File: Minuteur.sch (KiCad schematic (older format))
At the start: 40 parts, among them J1 ICSP, J2 Screw_Terminal_1x02, J3 Piezo, J4 Inputs, J5 Data, J6 USB_OTG, J7 Screw_Terminal_1x03, J8 Outputs, Q1 BC818-40, SW1 Rotary_Encoder_Switch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

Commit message: Commit last changes (probably Kicad wanting me to update footprints library) before switching to V2, with a new shaape for the board.
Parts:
- removed AFF1: CC56-12, Displays_7-Segment:Cx56-12, symbol CC56-12
- removed C1, C4, C5: 100n, Capacitors_SMD:C_0805, symbol C
- removed C2, C3: 47u, Capacitors_SMD:CP_Elec_6.3x5.3, symbol CP
- removed D1, D4: D, Diodes_SMD:D_SOD-123, symbol D
- removed D2, D3: LED, LEDs:LED_0805, symbol LED
- removed J1: ICSP, Connectors:IDC_Header_Straight_6pins, symbol CONN_02X03
- removed J2: Screw_Terminal_1x02, Connectors:bornier2, symbol Screw_Terminal_1x02
- removed J3: Piezo, Pin_Headers:Pin_Header_Straight_1x02_Pitch2.54mm, symbol CONN_01X02
- removed J4: Inputs, Pin_Headers:Pin_Header_Straight_1x07_Pitch2.54mm, symbol CONN_01X07
- removed J5: Data, Pin_Headers:Pin_Header_Straight_1x06_Pitch2.54mm, symbol CONN_01X06
- removed J6: USB_OTG, Connectors:USB_Micro-B, symbol USB_OTG
- removed J7: Screw_Terminal_1x03, Connectors:bornier3, symbol Screw_Terminal_1x03
- removed J8: Outputs, Pin_Headers:Pin_Header_Straight_1x04_Pitch2.54mm, symbol Conn_01x04
- removed Q1: BC818-40, TO_SOT_Packages_SMD:SOT-23, symbol BC818-40
- removed R1, R11, R12, R4, R5, R7: 470, Resistors_SMD:R_0805, symbol R
- removed R10: 510, Resistors_SMD:R_0805, symbol R
- removed R2: 10K, Resistors_SMD:R_0805, symbol R
- removed R3, R8, R9: 1K, Resistors_SMD:R_0805, symbol R
- removed R6: 30K, Resistors_SMD:R_0805, symbol R
- removed RL1: RelaySongle240VAC10A, Relays_THT:Relay_SPDT_SANYOU_SRD_Series_Form_C, symbol RelaySongle240VAC10A
- removed SW1: Rotary_Encoder_Switch, Switches_perso:EC12_switch-RotaryEncoder, symbol Rotary_Encoder_Switch
- removed SW2, SW3: SW_Push_SPDT_2Leds, Switches_perso:SP86-THT-PushButton, symbol SW_Push_SPDT_2Leds
- removed U1: ATMEGA328P-AU, Housings_QFP:TQFP-32_7x7mm_Pitch0.8mm, symbol ATMEGA328P-AU
- removed U2: LD1117S50TR, TO_SOT_Packages_SMD:SOT-223-3Lead_TabPin2, symbol LD1117S50TR
- removed U3: MAX7219, Housings_SOIC:SOIC-24W_7.5x15.4mm_Pitch1.27mm, symbol MAX7219
- removed U4: PC817, Housings_DIP:DIP-4_W7.62mm_SMD, symbol PC817
- removed Y1: 16MHz, SMD_perso:Resonator_SMD-3pin_3213, symbol Crystal_GND2
- added C1, C4, C5: 100n, Capacitor_SMD:C_0805_2012Metric, symbol Device:C
- added C2, C3: 47u, symbol Device:CP
- added D1, D4: D, Diode_SMD:D_SOD-123, symbol Device:D
- added D2, D3: LED, LED_SMD:LED_0805_2012Metric, symbol Device:LED
- added J1: Screw_Terminal_01x02, symbol Connector:Screw_Terminal_01x02
- added J2: ICSP, symbol Connector_Generic:Conn_02x03_Odd_Even
- added J3: piezo, symbol Connector_Generic:Conn_01x02
- added J4: input, symbol Connector_Generic:Conn_01x07
- added J5: USB_OTG, symbol Connector:USB_OTG
- added J6: data, symbol Connector_Generic:Conn_01x06
- added J7: output, symbol Connector_Generic:Conn_01x04
- added J8: Screw_Terminal_01x03, symbol Connector:Screw_Terminal_01x03
- added Q1: BC818, Package_TO_SOT_SMD:SOT-23, symbol Transistor_BJT:BC818
- added R1, R11, R4, R5, R7: 470, symbol Device:R
- added R10: 510, symbol Device:R
- added R2: 10k, symbol Device:R
- added R3, R8, R9: 1k, symbol Device:R
- added R6: 30k, symbol Device:R
- added RL1: RelaySongle240VAC10A, symbol Switch_Perso:RelaySongle240VAC10A
- added SW1: Rotary_Encoder_Switch, symbol Device:Rotary_Encoder_Switch
- added SW2: SW_Push_SPDT_2Leds, symbol Switch_Perso:SW_Push_SPDT_2Leds
- added U1: ATmega328P-AU, Package_QFP:TQFP-32_7x7mm_P0.8mm, symbol MCU_Microchip_ATmega:ATmega328P-AU
- added U2: LD1117S50TR_SOT223, Package_TO_SOT_SMD:SOT-223-3_TabPin2, symbol Regulator_Linear:LD1117S50TR_SOT223
- added U3: MAX7219, symbol Driver_LED:MAX7219
- added U4: PC817, Package_DIP:DIP-4_W7.62mm, symbol Isolator:PC817
- added U5: CC56-12EWA, Display_7Segment:CA56-12EWA, symbol Display_Character:CC56-12EWA
- added Y1: 16MHz, symbol Device:Crystal_GND2
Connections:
- wire segments 126 -> 118
- no-connect marks 21 -> 16

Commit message: General layout done.
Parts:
- removed D2, D3: LED, LED_SMD:LED_0805_2012Metric, symbol Device:LED
- removed J4: input, symbol Connector_Generic:Conn_01x07
- removed J5: USB_OTG, symbol Connector:USB_OTG
- removed J6: data, symbol Connector_Generic:Conn_01x06
- removed R3: 1k, symbol Device:R
- added C1: 100n, Capacitor_SMD:C_0805_2012Metric, symbol Device:C
- added FID1, FID2, FID3, FID4, FID5, FID6: Fiducial, Fiducial:Fiducial_0.75mm_Mask1.5mm, symbol Mechanical:Fiducial
- added H1, H2, H3, H4: MountingHole, MountingHole:MountingHole_3.2mm_M3, symbol Mechanical:MountingHole
- added J4: Conn_01x10, Connector_PinHeader_2.54mm:PinHeader_1x10_P2.54mm_Vertical, symbol Connector_Generic:Conn_01x10
- C3: renamed from C2; footprint (none) -> Capacitor_SMD:CP_Elec_6.3x5.3
- C4: renamed from C3; footprint (none) -> Capacitor_SMD:CP_Elec_6.3x5.3
- J1: footprint (none) -> Connector_Phoenix_MSTB:PhoenixContact_MSTBVA_2,5_2-G-5,08_1x02_P5.08mm_Vertical
- J2: footprint (none) -> Connector_PinHeader_2.54mm:PinHeader_2x03_P2.54mm_Vertical
- J3: footprint (none) -> Connector_PinHeader_2.54mm:PinHeader_1x02_P2.54mm_Vertical
- J5: renamed from J7; footprint (none) -> Connector_PinHeader_2.54mm:PinHeader_1x04_P2.54mm_Vertical
- J6: renamed from J8; footprint (none) -> Connector_Phoenix_MSTB:PhoenixContact_MSTBVA_2,5_3-G-5,08_1x03_P5.08mm_Vertical
- R1, R2: footprint (none) -> Resistor_SMD:R_0805_2012Metric
- R10: renamed from R11; footprint (none) -> Resistor_SMD:R_0805_2012Metric
- R3: renamed from R4; footprint (none) -> Resistor_SMD:R_0805_2012Metric
- R4: renamed from R5; footprint (none) -> Resistor_SMD:R_0805_2012Metric
- R5: renamed from R6; footprint (none) -> Resistor_SMD:R_0805_2012Metric
- R6: renamed from R7; footprint (none) -> Resistor_SMD:R_0805_2012Metric
- R7: renamed from R8; footprint (none) -> Resistor_SMD:R_0805_2012Metric
- R8: renamed from R9; footprint (none) -> Resistor_SMD:R_0805_2012Metric
- R9: renamed from R10; footprint (none) -> Resistor_SMD:R_0805_2012Metric
- RL1: footprint (none) -> Relay_THT:Relay_SPDT_SANYOU_SRD_Series_Form_C
- SW1: footprint (none) -> Rotary_Encoder:RotaryEncoder_Alps_EC12E-Switch_Vertical_H20mm_CircularMountingHoles
- SW2: footprint (none) -> Switch_Perso:SP86-THT-PushButton
- U3: footprint (none) -> Package_SO:SOIC-24W_7.5x15.4mm_P1.27mm
- Y1: footprint (none) -> Crystal:Resonator_SMD_muRata_CSTxExxV-3Pin_3.0x1.1mm
- renumbered C1 to C2, C4 to C5, C5 to C6, D4 to D2
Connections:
- net labels added: +12V, A3, A4, A5, A6, A7, D0, D1, D6
- net labels removed: BTN_3, RXD, SCL, SDA, TXD, VCC
- wire segments 118 -> 96
- no-connect marks 16 -> 10
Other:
- moved on the sheet: D1, J6, R2

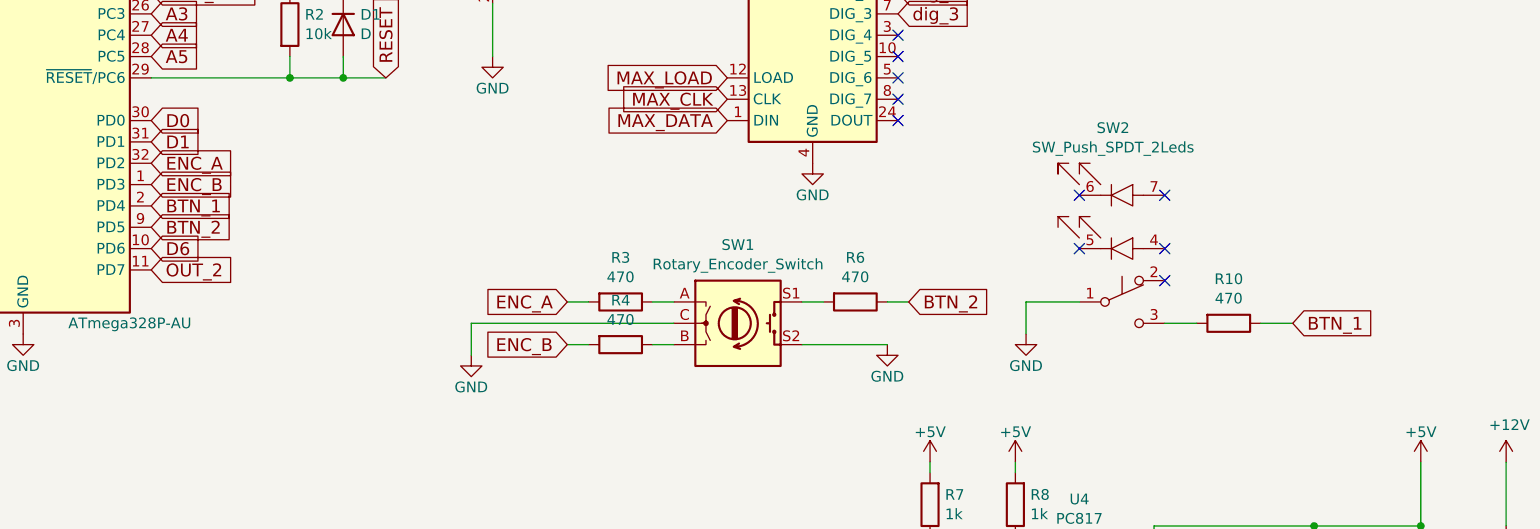
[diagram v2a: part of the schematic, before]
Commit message: Routing done. Maybe need to move down extension connectors a little. Also need to replace the piezo connector by a SMD one.
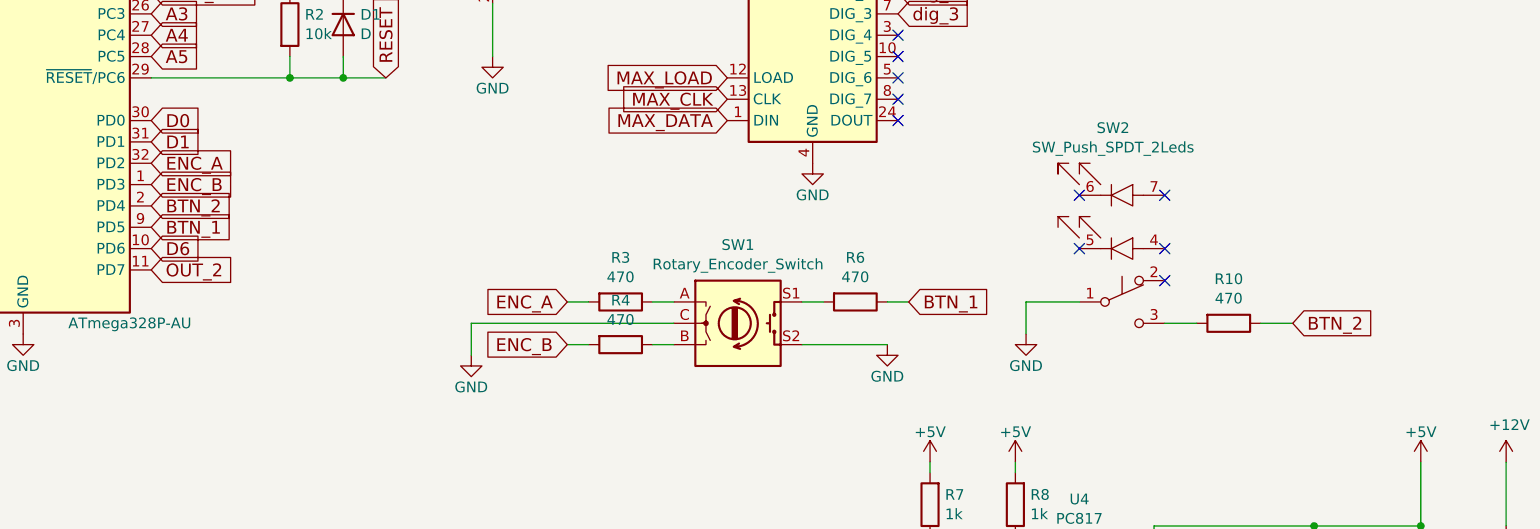
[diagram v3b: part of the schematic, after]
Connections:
- net BTN_1: now also R6.1, U1.9 (PD5); no longer R10.1, U1.2 (PD4)
- net BTN_2: now also R10.1, U1.2 (PD4); no longer R6.1, U1.9 (PD5)
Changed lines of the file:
@@
 ENC_A
 Text GLabel 3150 3800 2    60   Input ~ 0
-BTN_2
+BTN_1
 Text GLabel 3150 2500 2    60   Input ~ 0
 MAX_DATA
@@
 $EndComp
 Text GLabel 8500 4250 2    60   Input ~ 0
-BTN_1
+BTN_2
 $Comp
 L power:GND #PWR02
@@
 PIEZO_1
 Text GLabel 3150 3700 2    60   Input ~ 0
-BTN_1
+BTN_2
 $Comp
 L power:GND #PWR021
@@
 $EndComp
 $Comp
-L Connector_Generic:Conn_01x02 J3
-U 1 1 5EFB8BD6
-P 2050 5500
-F 0 "J3" H 2130 5492 50  0000 L CNN
-F 1 "piezo" H 2130 5401 50  0000 L CNN
-F 2 "Connector_PinHeader_2.54mm:PinHeader_1x02_P2.54mm_Vertical" H 2050 5500 50  0001 C CNN
-F 3 "~" H 2050 5500 50  0001 C CNN
-	1    2050 5500
-	1    0    0    -1
-$EndComp
-$Comp
 L Regulator_Linear:LD1117S50TR_SOT223 U2
 U 1 1 5EFBB817
@@
 Connection ~ 3350 6350
 Text GLabel 6700 4150 2    60   Input ~ 0
-BTN_2
+BTN_1
 Connection ~ 3800 2650
 $Comp
@@
 Wire Wire Line
 	1050 1600 1350 1600
+$Comp
+L Connector_Generic:Conn_01x02 J3
+U 1 1 5EFB8BD6
+P 2050 5500
+F 0 "J3" H 2130 5492 50  0000 L CNN
+F 1 "piezo" H 2130 5401 50  0000 L CNN
+F 2 "Connector_PinHeader_2.54mm:PinHeader_1x02_P2.54mm_Vertical" H 2050 5500 50  0001 C CNN
+F 3 "~" H 2050 5500 50  0001 C CNN
+	1    2050 5500
+	1    0    0    -1
+$EndComp
 $EndSCHEMATC

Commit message: All routing done, DRC ok.
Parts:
- removed J3: piezo, Connector_PinHeader_2.54mm:PinHeader_1x02_P2.54mm_Vertical, symbol Connector_Generic:Conn_01x02
- added U6: Piezo_sounder, IC_Perso:Murata_PKMCS0909_xxxxx, symbol Chip_Perso:Piezo_sounder
- R1: value 470 -> 1k
- R8: value 1k -> 470
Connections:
- net PIEZO_2: now also U6.2
- net at R1.1: now also U6.1
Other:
- moved on the sheet: R1
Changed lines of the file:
@@
 Text GLabel 3150 1700 2    60   Input ~ 0
 PIEZO_2
-Text GLabel 1350 5450 0    60   Input ~ 0
+Text GLabel 1950 5400 0    60   Input ~ 0
 PIEZO_1
 Text GLabel 3150 3700 2    60   Input ~ 0
@@
 	1    0    0    -1
 $EndComp
-Text GLabel 1350 5650 0    60   Input ~ 0
+Text GLabel 1950 5700 0    60   Input ~ 0
 PIEZO_2
 Wire Wire Line
@@
 Wire Wire Line
 	4950 2200 4950 2550
-Wire Wire Line
-	1350 5650 1800 5650
-Wire Wire Line
-	1800 5650 1800 5600
-Wire Wire Line
-	1800 5600 1850 5600
-Wire Wire Line
-	1350 5450 1450 5450
-Wire Wire Line
-	1750 5450 1800 5450
-Wire Wire Line
-	1800 5450 1800 5500
-Wire Wire Line
-	1800 5500 1850 5500
 Text GLabel 3150 1800 2    60   Input ~ 0
 PIEZO_1
@@
 P 7200 5100
 F 0 "R8" H 7130 5054 50  0000 R CNN
-F 1 "1k" H 7130 5145 50  0000 R CNN
+F 1 "470" H 7130 5145 50  0000 R CNN
 F 2 "Resistor_SMD:R_0805_2012Metric" V 7130 5100 50  0001 C CNN
 F 3 "~" H 7200 5100 50  0001 C CNN
@@
 Connection ~ 9100 5200
 $Comp
-L Device:R R1
-U 1 1 5EF81C42
-P 1600 5450
-F 0 "R1" V 1393 5450 50  0000 C CNN
-F 1 "470" V 1484 5450 50  0000 C CNN
-F 2 "Resistor_SMD:R_0805_2012Metric" V 1530 5450 50  0001 C CNN
-F 3 "~" H 1600 5450 50  0001 C CNN
-	1    1600 5450
-	0    1    1    0
-$EndComp
-$Comp
 L Device:C C5
 U 1 1 5EF86361
@@
 U 1 1 5EFADC83
 P 7500 5400
-F 0 "U4" H 7500 5725 50  0000 C CNN
-F 1 "PC817" H 7500 5634 50  0000 C CNN
+F 0 "U4" H 7300 5200 50  0000 C CNN
+F 1 "PC817" H 7600 5200 50  0000 C CNN
 F 2 "Package_DIP:DIP-4_W7.62mm" H 7300 5200 50  0001 L CIN
 F 3 "http://www.soselectronic.cz/a_info/resource/d/pc817.pdf" H 7500 5400 50  0001 L CNN
@@
 	1050 1600 1350 1600
 $Comp
-L Connector_Generic:Conn_01x02 J3
-U 1 1 5EFB8BD6
-P 2050 5500
-F 0 "J3" H 2130 5492 50  0000 L CNN
-F 1 "piezo" H 2130 5401 50  0000 L CNN
-F 2 "Connector_PinHeader_2.54mm:PinHeader_1x02_P2.54mm_Vertical" H 2050 5500 50  0001 C CNN
-F 3 "~" H 2050 5500 50  0001 C CNN
-	1    2050 5500
-	1    0    0    -1
+L Device:R R1
+U 1 1 5EF81C42
+P 2250 5400
+F 0 "R1" V 2043 5400 50  0000 C CNN
+F 1 "1k" V 2134 5400 50  0000 C CNN
+F 2 "Resistor_SMD:R_0805_2012Metric" V 2180 5400 50  0001 C CNN
+F 3 "~" H 2250 5400 50  0001 C CNN
+	1    2250 5400
+	0    1    1    0
+$EndComp
+Wire Wire Line
+	2400 5400 2600 5400
+Wire Wire Line
+	1950 5700 2600 5700
+Wire Wire Line
+	2100 5400 1950 5400
+$Comp
+L Chip_Perso:Piezo_sounder U6
+U 1 1 5FCD1C61
+P 2600 5550
+F 0 "U6" V 2547 5653 60  0000 L CNN
+F 1 "Piezo_sounder" V 2653 5653 60  0000 L CNN
+F 2 "IC_Perso:Murata_PKMCS0909_xxxxx" H 2600 5550 60  0001 C CNN
+F 3 "https://www.murata.com/en-us/products/sound/sounder/pkmcs" H 2600 5550 60  0001 C CNN
+	1    2600 5550
+	0    1    1    0
 $EndComp
 $EndSCHEMATC

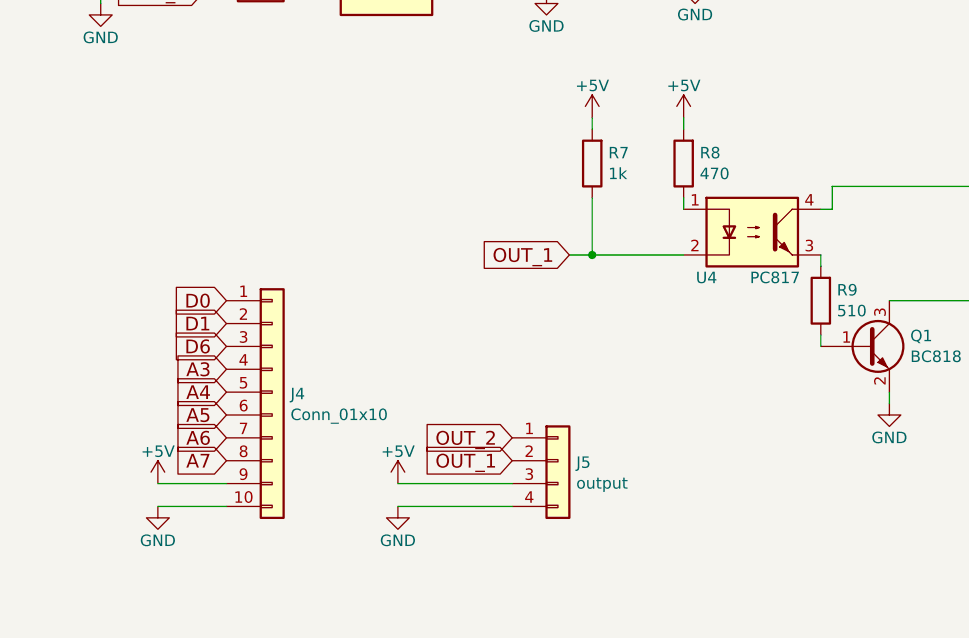
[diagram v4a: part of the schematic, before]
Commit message: Smaller version (100x50mm) routed. optocoupler changed. R-serie resistance for optocoupler changed to 200Ohm, so the optocoupler is in saturated region. Power lines have been changed from 0.25 to 0.5 width?
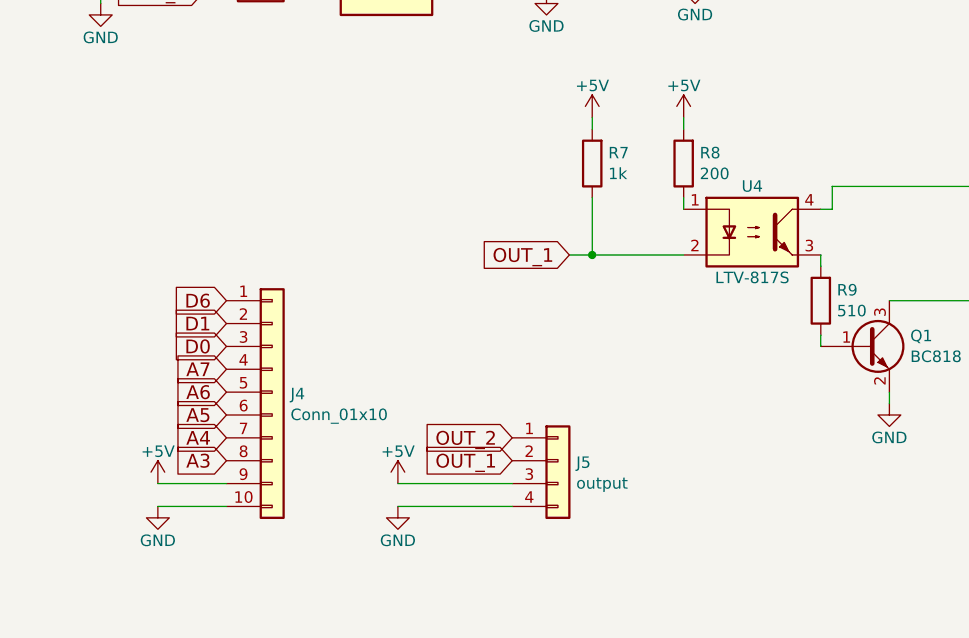
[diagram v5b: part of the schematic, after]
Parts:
- removed U4: PC817, Package_DIP:DIP-4_W7.62mm, symbol Isolator:PC817
- added U4: LTV-817S, Package_DIP:SMDIP-4_W9.53mm, symbol Isolator:LTV-817S
- R8: value 470 -> 200
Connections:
- net +5V: now also U4.4
- net A3: now also J4.8 (Pin_8); no longer J4.4 (Pin_4)
- net A4: now also J4.7 (Pin_7); no longer J4.5 (Pin_5)
- net A6: now also J4.5 (Pin_5); no longer J4.7 (Pin_7)
- net A7: now also J4.4 (Pin_4); no longer J4.8 (Pin_8)
- net D0: now also J4.3 (Pin_3); no longer J4.1 (Pin_1)
- net D6: now also J4.1 (Pin_1); no longer J4.3 (Pin_3)
- net OUT_1: now also U4.2
- net at R8.1: now also U4.1
- net at R9.2: now also U4.3
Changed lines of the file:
@@
 P 7200 5100
 F 0 "R8" H 7130 5054 50  0000 R CNN
-F 1 "470" H 7130 5145 50  0000 R CNN
+F 1 "200" H 7130 5145 50  0000 R CNN
 F 2 "Resistor_SMD:R_0805_2012Metric" V 7130 5100 50  0001 C CNN
 F 3 "~" H 7200 5100 50  0001 C CNN
@@
 $EndComp
 $Comp
-L Isolator:PC817 U4
-U 1 1 5EFADC83
-P 7500 5400
-F 0 "U4" H 7300 5200 50  0000 C CNN
-F 1 "PC817" H 7600 5200 50  0000 C CNN
-F 2 "Package_DIP:DIP-4_W7.62mm" H 7300 5200 50  0001 L CIN
-F 3 "http://www.soselectronic.cz/a_info/resource/d/pc817.pdf" H 7500 5400 50  0001 L CNN
-	1    7500 5400
-	1    0    0    -1
-$EndComp
-$Comp
 L Device:R R9
 U 1 1 5EFB3CD0
@@
 	7200 5500 6800 5500
 Connection ~ 6800 5500
-Text GLabel 5200 6000 0    60   Input ~ 0
+Text GLabel 5200 6400 0    60   Input ~ 0
 A3
-Text GLabel 5200 6100 0    60   Input ~ 0
+Text GLabel 5200 6300 0    60   Input ~ 0
 A4
 Text GLabel 5200 6200 0    60   Input ~ 0
 A5
-Text GLabel 5200 6300 0    60   Input ~ 0
+Text GLabel 5200 6100 0    60   Input ~ 0
 A6
-Text GLabel 5200 6400 0    60   Input ~ 0
+Text GLabel 5200 6000 0    60   Input ~ 0
 A7
-Text GLabel 5200 5700 0    60   Input ~ 0
+Text GLabel 5200 5900 0    60   Input ~ 0
 D0
 Text GLabel 5200 5800 0    60   Input ~ 0
 D1
-Text GLabel 5200 5900 0    60   Input ~ 0
+Text GLabel 5200 5700 0    60   Input ~ 0
 D6
 $Comp
@@
 	0    1    1    0
 $EndComp
+$Comp
+L Isolator:LTV-817S U4
+U 1 1 5FCA56EC
+P 7500 5400
+F 0 "U4" H 7500 5600 50  0000 C CNN
+F 1 "LTV-817S" H 7500 5200 50  0000 C CNN
+F 2 "Package_DIP:SMDIP-4_W9.53mm" H 7500 5100 50  0001 C CNN
+F 3 "http://www.us.liteon.com/downloads/LTV-817-827-847.PDF" H 7150 5700 50  0001 C CNN
+	1    7500 5400
+	1    0    0    -1
+$EndComp
 $EndSCHEMATC

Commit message: AC version ready for fab.
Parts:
- removed C3, C4: 47u, Capacitor_SMD:CP_Elec_6.3x5.3, symbol Device:CP
- removed C5: 100n, Capacitor_SMD:C_0805_2012Metric, symbol Device:C
- removed J1: Screw_Terminal_01x02, Connector_Phoenix_MSTB:PhoenixContact_MSTBVA_2,5_2-G-5,08_1x02_P5.08mm_Vertical, symbol Connector:Screw_Terminal_01x02
- removed U2: LD1117S50TR_SOT223, Package_TO_SOT_SMD:SOT-223-3_TabPin2, symbol Regulator_Linear:LD1117S50TR_SOT223
- added J2: USB_B_Micro, Connector_USB:USB_Micro-B_Amphenol_10118194_Horizontal, symbol Connector:USB_B_Micro
- renumbered C6 to C3, J2 to J1, J4 to J3, J5 to J4, J6 to J5, U6 to U2
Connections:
- net +12V is gone; now on an unnamed net: RL1.1 (COM)
- net +5V: now also J2.1 (VBUS)
- net GND: now also J2.5 (GND), J2.6 (Shield); no longer J5.3 (Pin_3)
- net at J5.2 (Pin_2): no longer RL1.3 (NO)
- new net: J5.3 (Pin_3), RL1.3 (NO)
- no-connect marks 10 -> 13
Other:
- moved on the sheet: J5
